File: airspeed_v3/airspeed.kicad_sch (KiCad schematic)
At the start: 27 parts, among them J1 Header, J2 GPS, J3 GPS, J4 ScreenIO, U1 XGZP6897D, U3 SHT4x, U5 XGZP6897D, U6 BME280, U8 BMP280

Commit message: complete airspeed v3.2
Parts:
- removed J1: Header, Connector_PinHeader_2.54mm:PinHeader_1x06_P2.54mm_Vertical, symbol Connector:Conn_01x06_Pin
- removed J4: ScreenIO, Connector_PinHeader_1.27mm:PinHeader_1x08_P1.27mm_Vertical, symbol Connector:Conn_01x08_Pin
- removed R5: 10k, Resistor_SMD:R_0805_2012Metric, symbol Device:R
- removed U3: SHT4x, Sensor_Humidity:Sensirion_DFN-4_1.5x1.5mm_P0.8mm_SHT4x_NoCentralPad, symbol Sensor_Humidity:SHT4x
- added J1: Header, Connector_PinHeader_1.27mm:PinHeader_1x10_P1.27mm_Vertical, symbol Connector:Conn_01x10_Pin
- added R3: 10k, Resistor_SMD:R_0805_2012Metric, symbol Device:R
- JP1, JP2: value 0x76 | 0x77 -> 0x76|0x77; footprint Jumper:SolderJumper-3_P2.0mm_Open_TrianglePad1.0x1.5mm -> Jumper:SolderJumper-3_P1.3mm_Open_RoundedPad1.0x1.5mm
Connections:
- net +3V3: now also J1.10 (Pin_10), R3.1
- net 5V: now also J1.3 (Pin_3)
- net GND: now also J1.4 (Pin_4), J1.9 (Pin_9)
- net Rx: now also J1.6 (Pin_6)
- net SCL: now also J1.2 (Pin_2)
- net SCL2: now also J1.8 (Pin_8), R3.2; no longer R4.2
- net SDA: now also J1.1 (Pin_1)
- net SDA2: now also R4.2, J1.7 (Pin_7)
- net Tx: now also J1.5 (Pin_5)
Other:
- moved on the sheet: JP2, U8

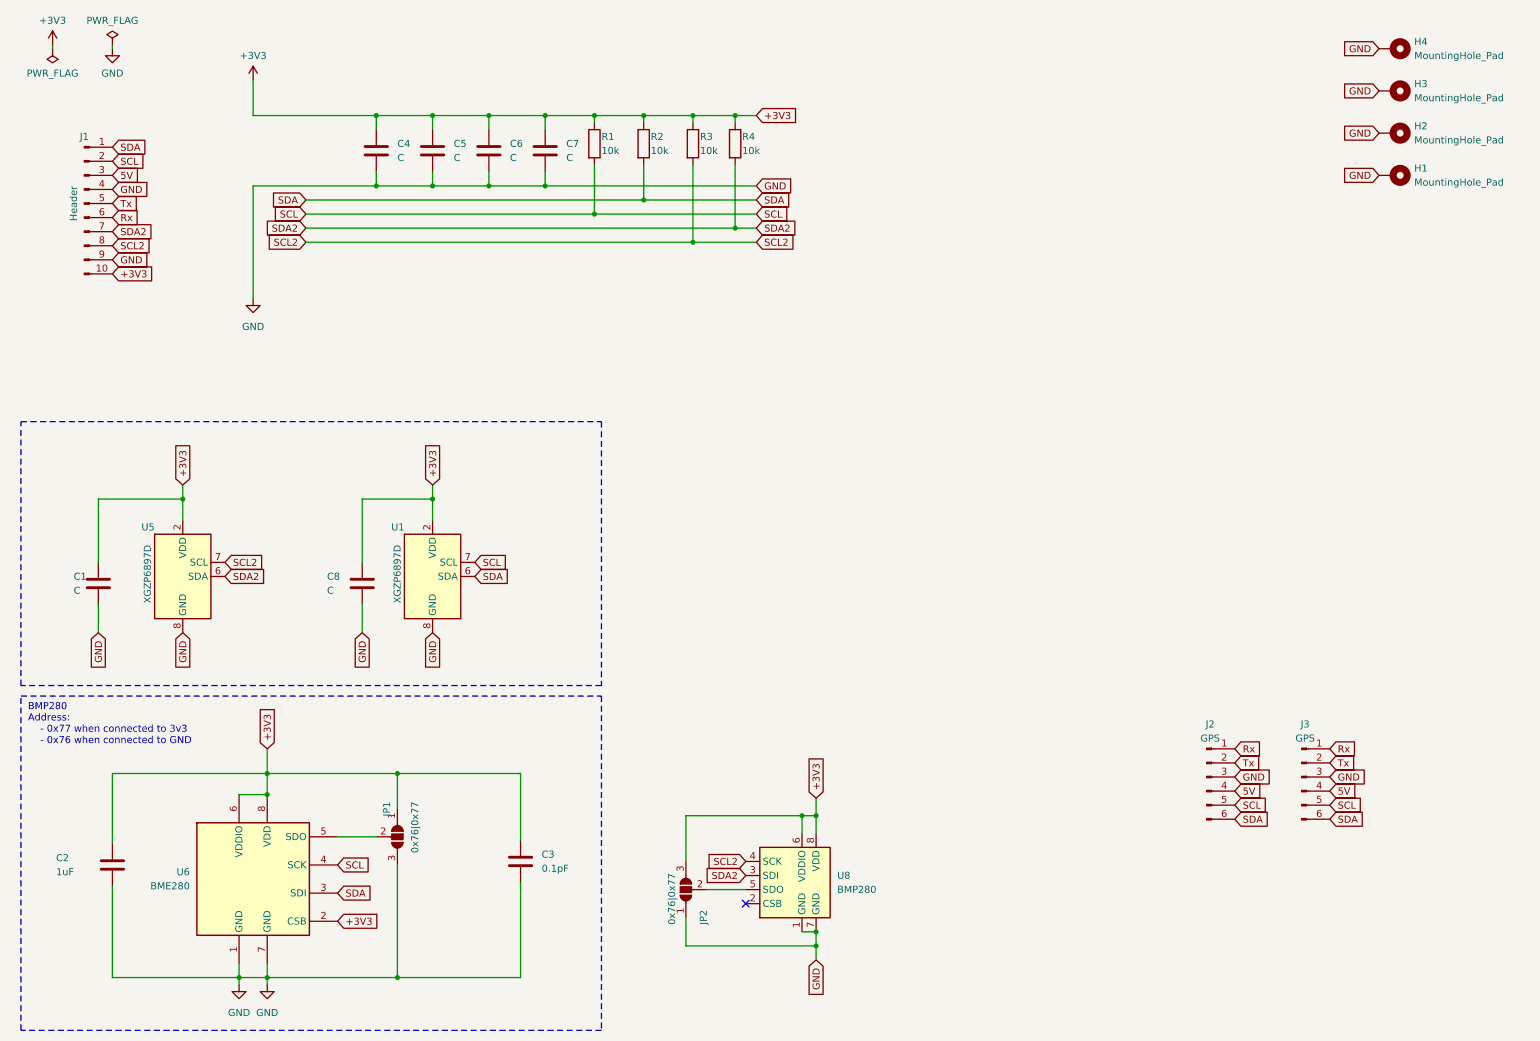
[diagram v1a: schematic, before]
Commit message: upgrade to kicad v8
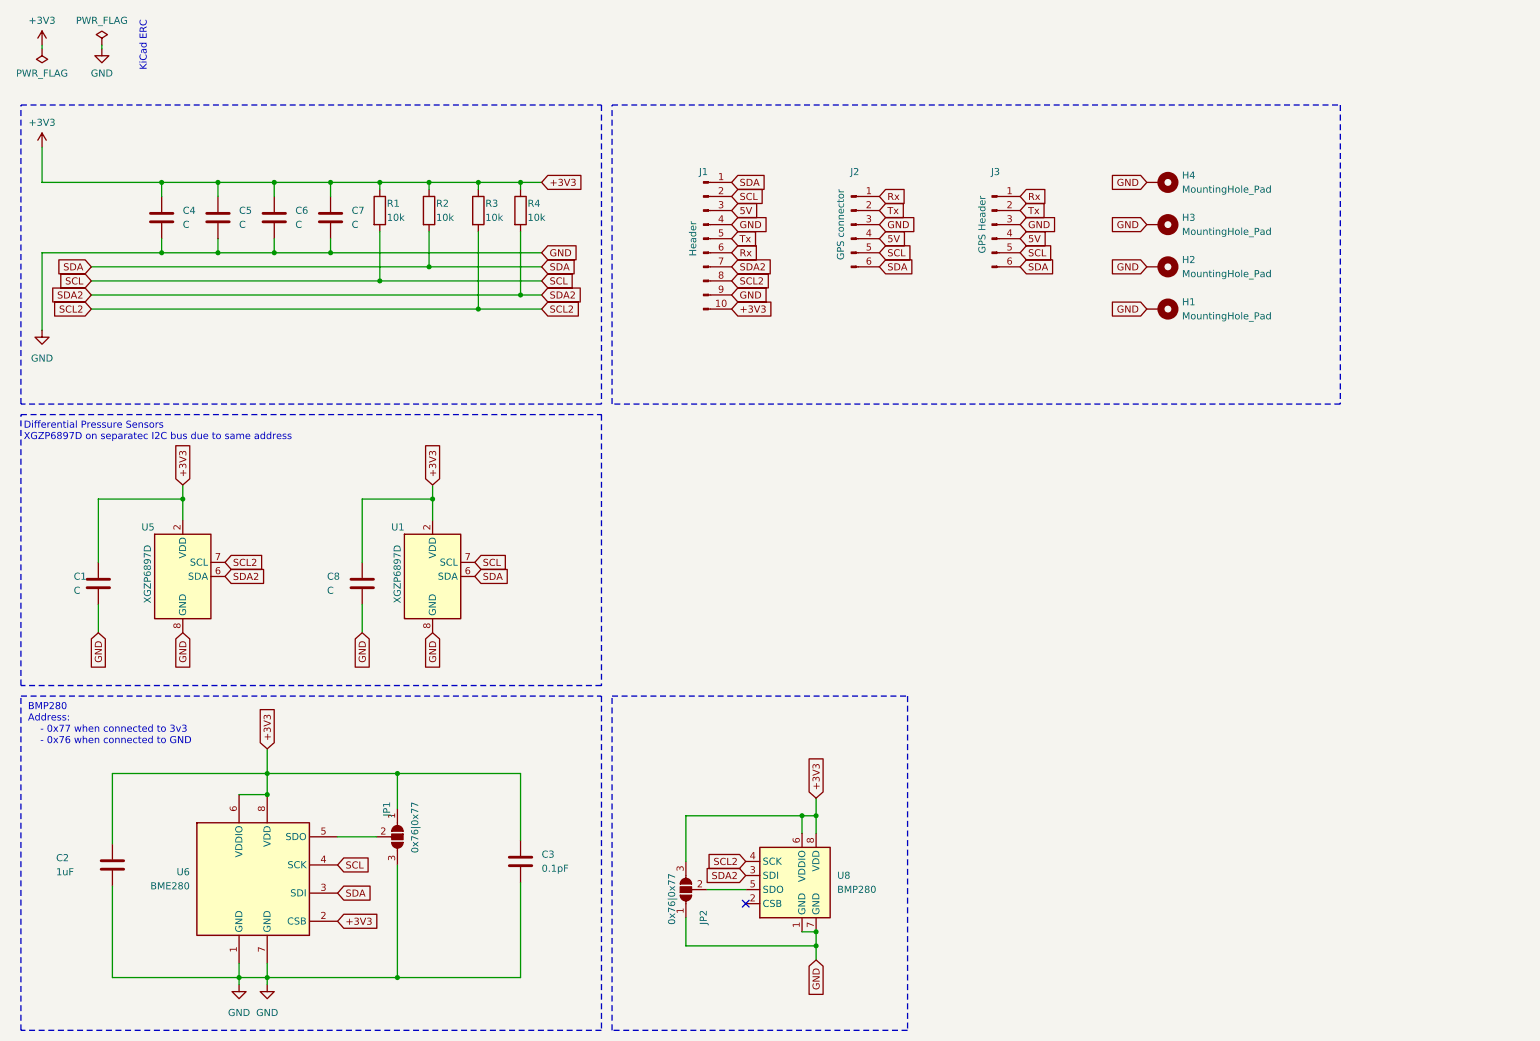
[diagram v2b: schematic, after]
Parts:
- J2: value GPS -> GPS connector
- J3: value GPS -> GPS Header
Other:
- note added: "Differential Pressure Sensors XGZP6897D on separatec I2C bus due to same address"
- note added: "KiCad ERC"
- moved on the sheet: C4, C5, C6, C7, H1, H2, H3, H4, J1, J2, J3, R1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

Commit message: updated the schematic to use latest bp280
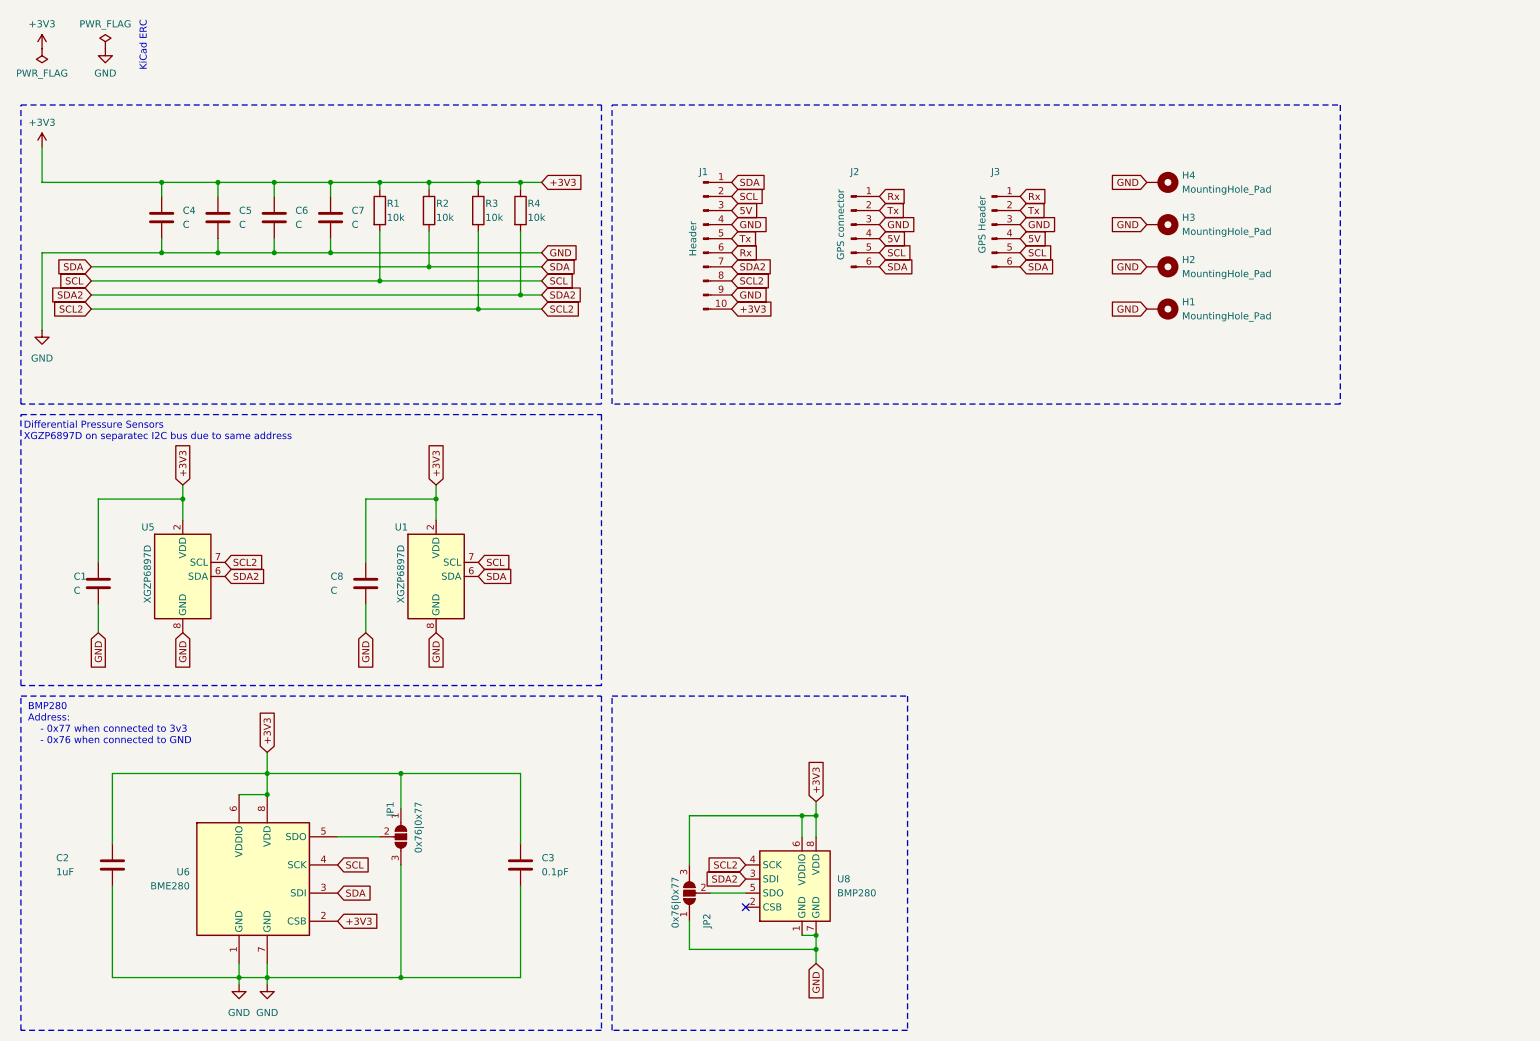
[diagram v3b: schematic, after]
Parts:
- removed U8: BMP280, Package_LGA:Bosch_LGA-8_2x2.5mm_P0.65mm_ClockwisePinNumbering, symbol Diff_Pressure:BMP280
- added U8: BMP280, Package_LGA:Bosch_LGA-8_2x2.5mm_P0.65mm_ClockwisePinNumbering, symbol Sensor_Pressure:BMP280
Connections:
- net +3V3: now also U8.6 (VDDIO), U8.8 (VDD)
- net GND: now also U8.1 (GND), U8.7 (GND)
- net SCL2: now also U8.4 (SCK)
- net SDA2: now also U8.3 (SDI)
- net at JP2.2 (C): now also U8.5 (SDO)
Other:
- moved on the sheet: C3, C8, JP1, JP2, U1
